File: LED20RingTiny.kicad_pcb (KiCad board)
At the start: 2 copper layers, 24 parts, among them IC1 ATTINY45-P, SW1 SW_Push

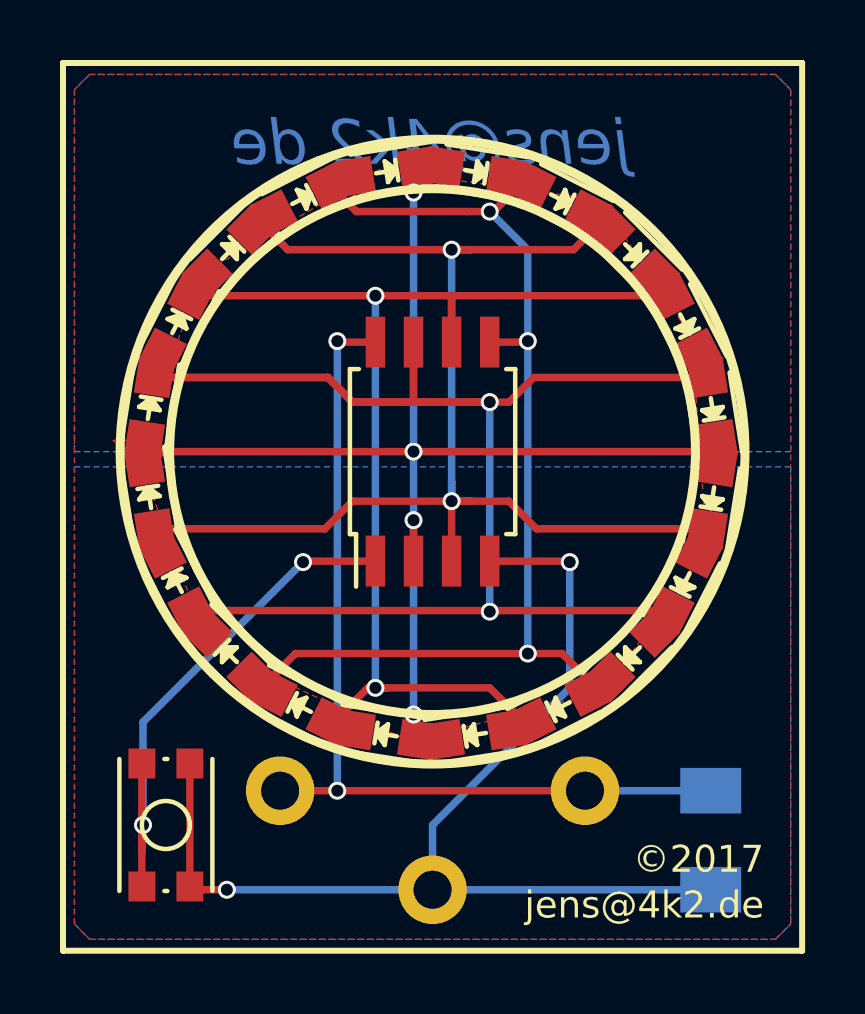
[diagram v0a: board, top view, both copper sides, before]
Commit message: Add Edge Cuts
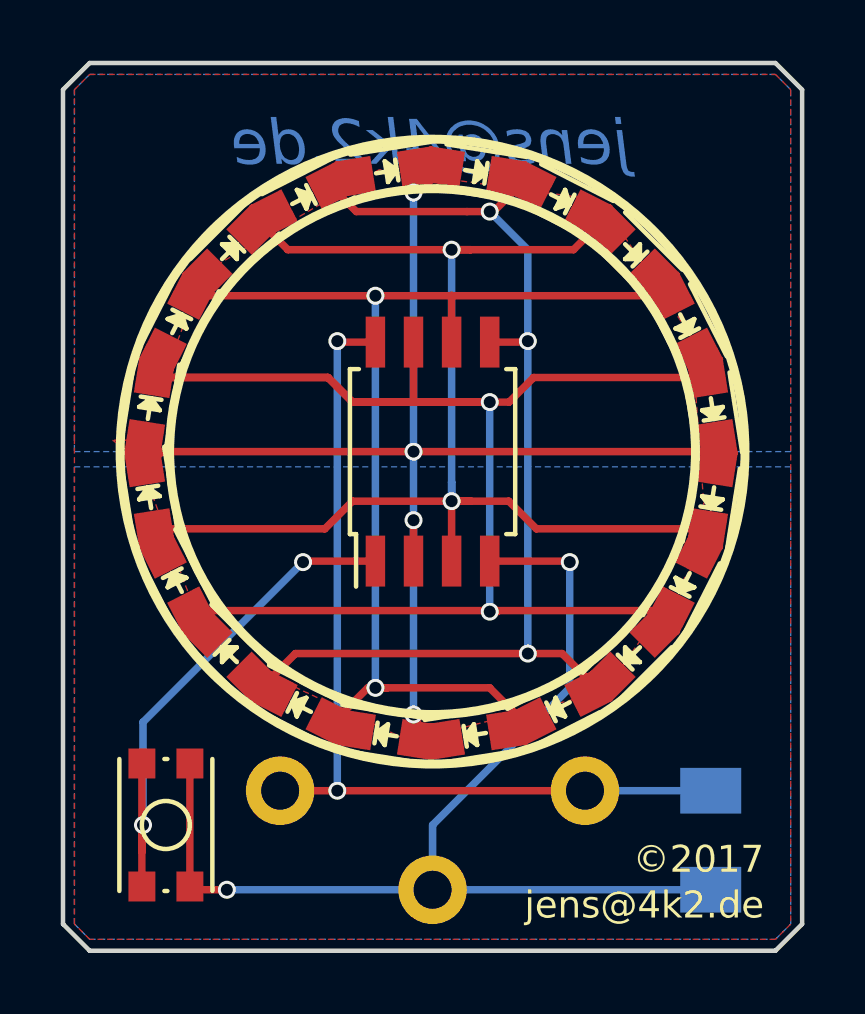
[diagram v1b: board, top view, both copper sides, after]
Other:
- board outline added: 24.6 x 29.6 mm
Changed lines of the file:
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@@
     (links 49)
     (no_connects 0)
-    (area 157.612014 86.894999 182.472001 116.686001)
+    (area 157.658999 86.919999 182.447001 116.661001)
     (thickness 1.6)
-    (drawings 10)
+    (drawings 13)
     (tracks 161)
     (zones 0)
@@
       (net 7 GND))
   )
+  (gr_line (start 157.734 115.697) (end 157.734 87.884) (angle 90) (layer Edge.Cuts) (width 0.15))
+  (gr_line (start 158.623 116.586) (end 157.734 115.697) (angle 90) (layer Edge.Cuts) (width 0.15))
+  (gr_line (start 181.483 116.586) (end 158.623 116.586) (angle 90) (layer Edge.Cuts) (width 0.15))
+  (gr_line (start 182.372 115.697) (end 181.483 116.586) (angle 90) (layer Edge.Cuts) (width 0.15))
+  (gr_line (start 182.372 87.884) (end 182.372 115.697) (angle 90) (layer Edge.Cuts) (width 0.15))
+  (gr_line (start 181.483 86.995) (end 182.372 87.884) (angle 90) (layer Edge.Cuts) (width 0.15))
+  (gr_line (start 158.623 86.995) (end 181.483 86.995) (angle 90) (layer Edge.Cuts) (width 0.15))
+  (gr_line (start 157.734 87.884) (end 158.623 86.995) (angle 90) (layer Edge.Cuts) (width 0.15))
   (gr_text jens@4k2.de (at 170.053 89.662) (layer B.Cu)
     (effects (font (size 1.5 1.5) (thickness 0.25) italic) (justify mirror))
@@
     (effects (font (size 0.9 0.9) (thickness 0.175)) (justify right))
   )
-  (gr_line (start 182.372 116.586) (end 157.734 116.586) (angle 90) (layer F.SilkS) (width 0.2))
-  (gr_line (start 182.372 86.995) (end 182.372 116.586) (angle 90) (layer F.SilkS) (width 0.2))
-  (gr_line (start 182.245 86.995) (end 182.372 86.995) (angle 90) (layer F.SilkS) (width 0.2))
-  (gr_line (start 157.734 86.995) (end 182.245 86.995) (angle 90) (layer F.SilkS) (width 0.2))
-  (gr_line (start 157.734 116.586) (end 157.734 86.995) (angle 90) (layer F.SilkS) (width 0.2))
   (segment (start 171.323 101.6) (end 170.688 101.6) (width 0.25) (layer F.Cu) (net 1))
   (via (at 170.688 101.6) (size 0.6) (drill 0.4) (layers F.Cu B.Cu) (net 1))
